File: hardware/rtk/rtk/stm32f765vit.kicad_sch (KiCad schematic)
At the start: 30 parts, among them J10 Conn_01x02_Pin, J6 MEM2052-00-195-00-A_REVA, J7 Conn_01x04_Pin, J8 Conn_01x01_Pin, J9 Conn_01x08_Pin, U3 STM32F765VITx, U5 ESP32-S3-ZERO, U6 CORE1262-868M, U7 LSM6DSOX, Y1 ASTX-H11-16.000MHZ-T

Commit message: Schematic fixes and PCB placement start: D2, C16/18/20, J4
- D2: PRTR5V0U2X → USBLC6-2SC6 (SOT-23-6), D3 removed
- C16/C18/C20: symbol → C_Polarized_Small, footprint → 0805 HandSolder
  (T529P106M010AAE200 polymer tant 10µF 10V)
- J4: footprint assigned (PinHeader 2.54mm, on/off switch)
- rtk.kicad_pcb: initial component placement begun
- Add USBLC6-2SC6 datasheet

Co-Authored-By: Claude Sonnet 4.6 <noreply@anthropic.com>
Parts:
- C16, C18, C20: footprint Capacitor_SMD:C_Elec_8x10.2 -> Capacitor_SMD:C_0805_2012Metric_Pad1.18x1.45mm_HandSolder
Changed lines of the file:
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@@
 			)
 		)
-		(property "Footprint" "Capacitor_SMD:C_Elec_8x10.2"
+		(property "Footprint" "Capacitor_SMD:C_0805_2012Metric_Pad1.18x1.45mm_HandSolder"
 			(at 269.24 133.35 0)
 			(hide yes)
@@
 			)
 		)
-		(property "Footprint" "Capacitor_SMD:C_Elec_8x10.2"
+		(property "Footprint" "Capacitor_SMD:C_0805_2012Metric_Pad1.18x1.45mm_HandSolder"
 			(at 269.24 87.63 0)
 			(hide yes)
@@
 			)
 		)
-		(property "Footprint" "Capacitor_SMD:C_Elec_8x10.2"
+		(property "Footprint" "Capacitor_SMD:C_0805_2012Metric_Pad1.18x1.45mm_HandSolder"
 			(at 269.24 36.83 0)
 			(hide yes)

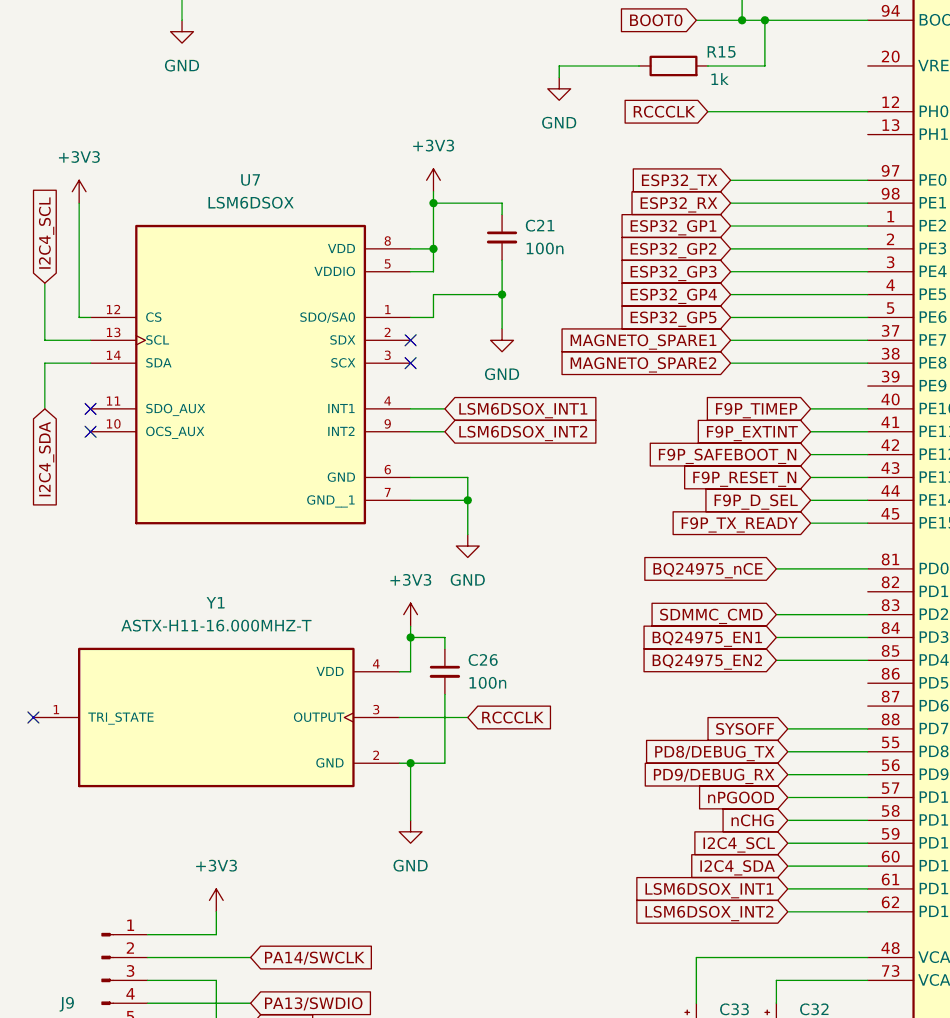
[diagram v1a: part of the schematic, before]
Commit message: PCB: round 1 initial placement complete
Most components in final positions; some will shift during routing.
Schematic tweaks picked up alongside. Add GCT USB4105 datasheet.

Co-Authored-By: Claude Sonnet 4.6 <noreply@anthropic.com>
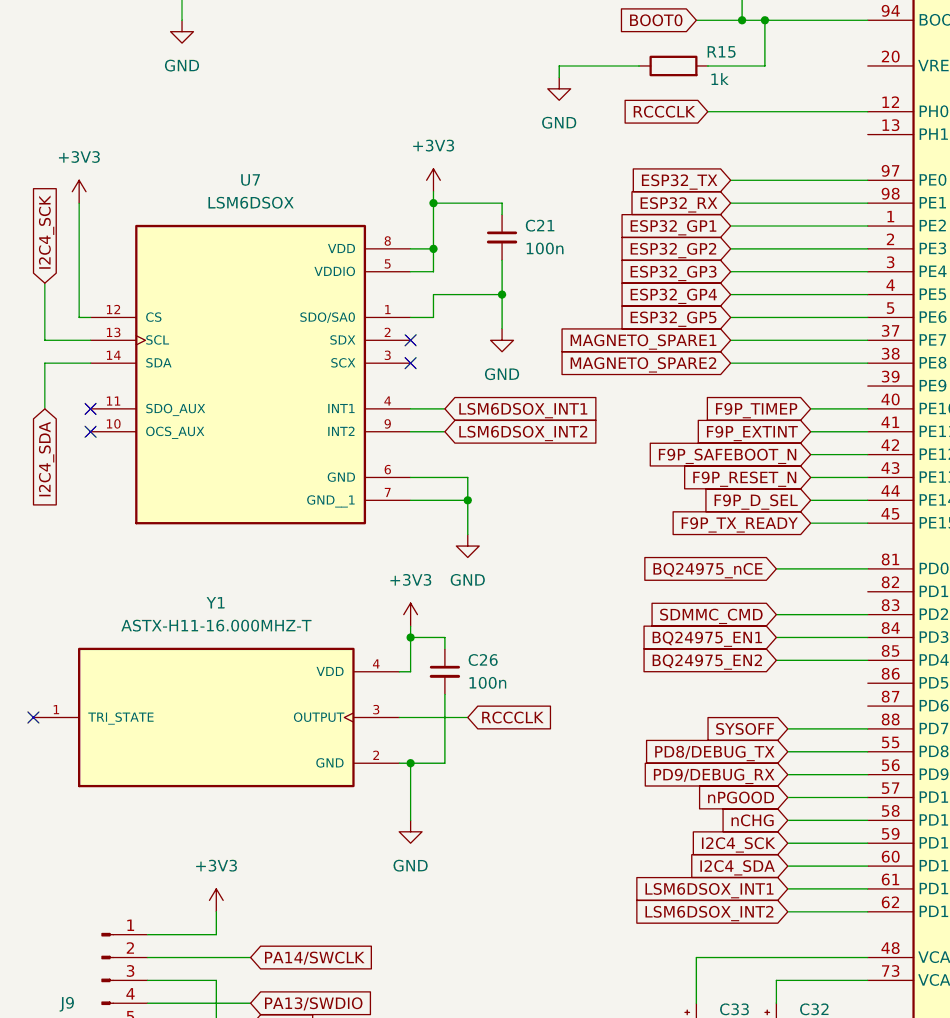
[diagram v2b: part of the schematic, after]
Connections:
- net I2C4_SCL is gone; now on net I2C4_SCK: U3.59 (PD12), U7.13 (SCL)
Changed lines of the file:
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@@
 		)
 	)
-	(global_label "I2C4_SCL"
+	(global_label "I2C4_SCK"
 		(shape input)
 		(at 99.06 137.16 180)
@@
 		)
 		(property "Intersheetrefs" "${INTERSHEET_REFS}"
-			(at 87.3058 137.16 0)
+			(at 87.0639 137.16 0)
 			(hide yes)
 			(show_name no)
@@
 		)
 	)
-	(global_label "I2C4_SCL"
+	(global_label "I2C4_SCK"
 		(shape input)
 		(at 16.51 74.93 90)
@@
 		)
 		(property "Intersheetrefs" "${INTERSHEET_REFS}"
-			(at 16.51 63.1758 90)
-			(hide yes)
-			(show_name no)
+			(at 16.51 62.9339 90)
+			(hide yes)
+			(show_name no)

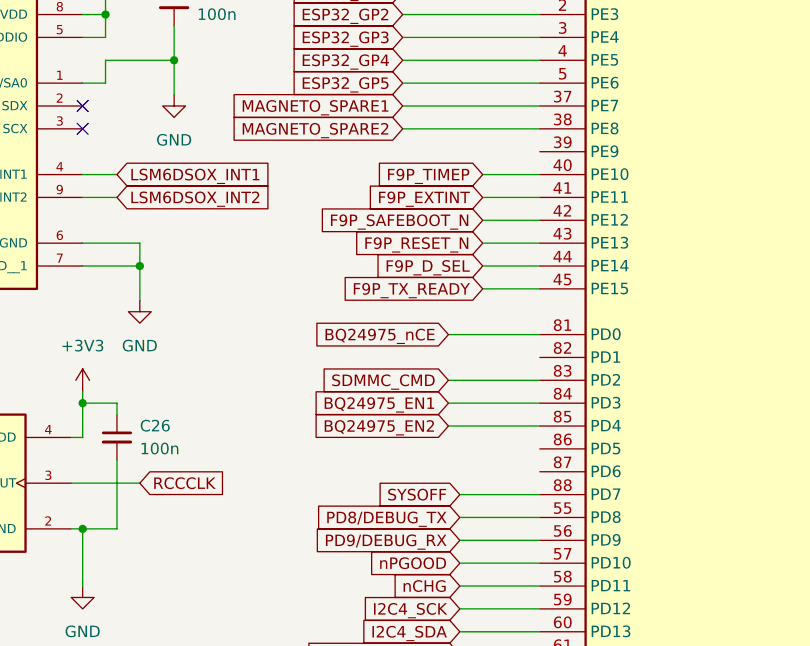
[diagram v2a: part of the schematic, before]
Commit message: Add LD3/LD4 debug LEDs: schematic, PCB placement, ioc
LD3 green PD5, LD4 red PD6 — open-drain outputs, R20/R21 1k5 pull-ups.
CubeMX regenerated with PD5/PD6 configured. Ready for routing.

Co-Authored-By: Claude Sonnet 4.6 <noreply@anthropic.com>
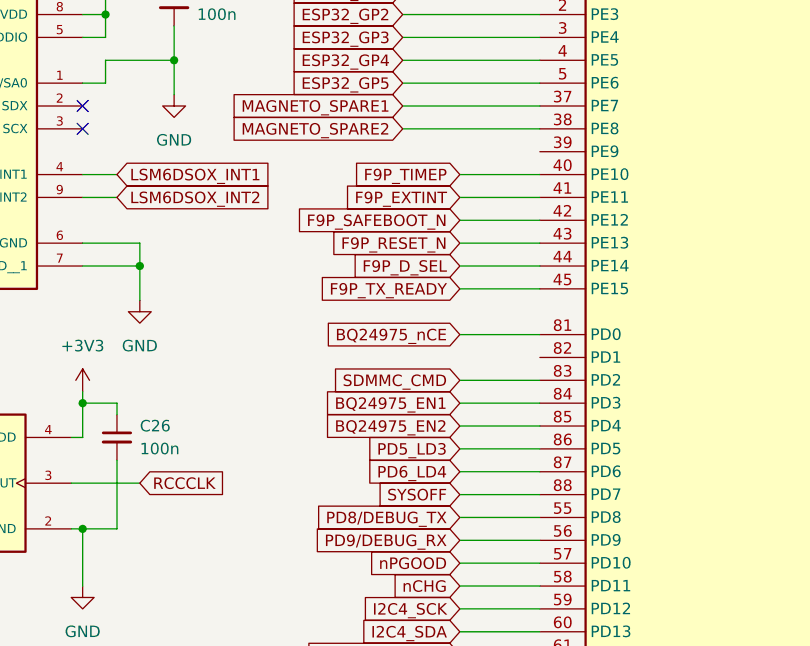
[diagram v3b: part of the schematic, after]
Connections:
- net PD5_LD3: now reaches U3.86 (PD5)
- net PD6_LD4: now reaches U3.87 (PD6)
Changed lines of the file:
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@@
 	(wire
 		(pts
-			(xy 101.6 88.9) (xy 107.95 88.9)
+			(xy 99.06 88.9) (xy 107.95 88.9)
 		)
 		(stroke
@@
 	(wire
 		(pts
-			(xy 101.6 96.52) (xy 107.95 96.52)
+			(xy 99.06 96.52) (xy 107.95 96.52)
 		)
 		(stroke
@@
 	(wire
 		(pts
-			(xy 101.6 99.06) (xy 107.95 99.06)
+			(xy 99.06 99.06) (xy 107.95 99.06)
 		)
 		(stroke
@@
 	(wire
 		(pts
+			(xy 99.06 119.38) (xy 107.95 119.38)
+		)
+		(stroke
+			(width 0)
+			(type default)
+		)
+	)
+	(wire
+		(pts
 			(xy 99.06 127) (xy 107.95 127)
 		)
@@
 	(wire
 		(pts
-			(xy 101.6 93.98) (xy 107.95 93.98)
+			(xy 99.06 93.98) (xy 107.95 93.98)
 		)
 		(stroke
@@
 	(wire
 		(pts
-			(xy 101.6 91.44) (xy 107.95 91.44)
+			(xy 99.06 91.44) (xy 107.95 91.44)
 		)
 		(stroke
@@
 	(wire
 		(pts
-			(xy 97.79 106.68) (xy 107.95 106.68)
+			(xy 99.06 106.68) (xy 107.95 106.68)
 		)
 		(stroke
@@
 	(wire
 		(pts
-			(xy 101.6 101.6) (xy 107.95 101.6)
+			(xy 99.06 101.6) (xy 107.95 101.6)
 		)
 		(stroke
@@
 	(wire
 		(pts
-			(xy 97.79 111.76) (xy 107.95 111.76)
+			(xy 99.06 111.76) (xy 107.95 111.76)
 		)
 		(stroke
@@
 	(wire
 		(pts
-			(xy 97.79 114.3) (xy 107.95 114.3)
+			(xy 99.06 114.3) (xy 107.95 114.3)
 		)
 		(stroke
@@
 	(wire
 		(pts
+			(xy 99.06 121.92) (xy 107.95 121.92)
+		)
+		(stroke
+			(width 0)
+			(type default)
+		)
+	)
+	(wire
+		(pts
 			(xy 55.88 128.27) (xy 57.15 128.27)
 		)
@@
 	(wire
 		(pts
-			(xy 97.79 116.84) (xy 107.95 116.84)
+			(xy 99.06 116.84) (xy 107.95 116.84)
 		)
 		(stroke
@@
 	(global_label "BQ24975_nCE"
 		(shape input)
-		(at 97.79 106.68 180)
+		(at 99.06 106.68 180)
 		(fields_autoplaced yes)
 		(effects
@@
 		)
 		(property "Intersheetrefs" "${INTERSHEET_REFS}"
-			(at 81.6212 106.68 0)
+			(at 82.8912 106.68 0)
 			(hide yes)
 			(show_name no)
@@
 	(global_label "F9P_SAFEBOOT_N"
 		(shape input)
-		(at 101.6 93.98 180)
+		(at 99.06 93.98 180)
 		(fields_autoplaced yes)
 		(effects
@@
 		)
 		(property "Intersheetrefs" "${INTERSHEET_REFS}"
-			(at 82.3467 93.98 0)
+			(at 79.8067 93.98 0)
 			(hide yes)
 			(show_name no)
@@
 		)
 	)
+	(global_label "PD6_LD4"
+		(shape input)
+		(at 99.06 121.92 180)
+		(fields_autoplaced yes)
+		(effects
+			(font
+				(size 1.27 1.27)
+			)
+			(justify right)
+		)
+		(property "Intersheetrefs" "${INTERSHEET_REFS}"
+			(at 87.8501 121.92 0)
+			(hide yes)
+			(show_name no)
+			(do_not_autoplace no)
+			(effects
+				(font
+					(size 1.27 1.27)
+				)
+				(justify right)
+			)
+		)
+	)
 	(global_label "SX1262_SPI2_MOSI"
 		(shape input)
@@
 	(global_label "F9P_TX_READY"
 		(shape input)
-		(at 101.6 101.6 180)
+		(at 99.06 101.6 180)
 		(fields_autoplaced yes)
 		(effects
@@
 		)
 		(property "Intersheetrefs" "${INTERSHEET_REFS}"
-			(at 85.0682 101.6 0)
+			(at 82.5282 101.6 0)
 			(hide yes)
 			(show_name no)
@@
 	(global_label "SDMMC_CMD"
 		(shape input)
-		(at 97.79 111.76 180)
+		(at 99.06 111.76 180)
 		(fields_autoplaced yes)
 		(effects
@@
 		)
 		(property "Intersheetrefs" "${INTERSHEET_REFS}"
-			(at 83.1935 111.76 0)
+			(at 84.4635 111.76 0)
 			(hide yes)
 			(show_name no)
@@
 	(global_label "F9P_RESET_N"
 		(shape input)
-		(at 101.6 96.52 180)
+		(at 99.06 96.52 180)
 		(fields_autoplaced yes)
 		(effects
@@
 		)
 		(property "Intersheetrefs" "${INTERSHEET_REFS}"
-			(at 86.0359 96.52 0)
+			(at 83.4959 96.52 0)
 			(hide yes)
 			(show_name no)
@@
 	(global_label "F9P_D_SEL"
 		(shape input)
-		(at 101.6 99.06 180)
+		(at 99.06 99.06 180)
 		(fields_autoplaced yes)
 		(effects
@@
 		)
 		(property "Intersheetrefs" "${INTERSHEET_REFS}"
-			(at 88.4549 99.06 0)
+			(at 85.9149 99.06 0)
 			(hide yes)
 			(show_name no)
@@
 		)
 	)
+	(global_label "PD5_LD3"
+		(shape input)
+		(at 99.06 119.38 180)
+		(fields_autoplaced yes)
+		(effects
+			(font
+				(size 1.27 1.27)
+			)
+			(justify right)
+		)
+		(property "Intersheetrefs" "${INTERSHEET_REFS}"
+			(at 87.8501 119.38 0)
+			(hide yes)
+			(show_name no)
+			(do_not_autoplace no)
+			(effects
+				(font
+					(size 1.27 1.27)
+				)
+				(justify right)
+			)
+		)
+	)
 	(global_label "F9P_ANT_SHORT"
 		(shape input)
@@
 	(global_label "F9P_EXTINT"
 		(shape input)
-		(at 101.6 91.44 180)
+		(at 99.06 91.44 180)
 		(fields_autoplaced yes)
 		(effects
@@
 		)
 		(property "Intersheetrefs" "${INTERSHEET_REFS}"
-			(at 87.8501 91.44 0)
+			(at 85.3101 91.44 0)
 			(hide yes)
 			(show_name no)
@@
 	(global_label "BQ24975_EN1"
 		(shape input)
-		(at 97.79 114.3 180)
+		(at 99.06 114.3 180)
 		(fields_autoplaced yes)
 		(effects
@@
 		)
 		(property "Intersheetrefs" "${INTERSHEET_REFS}"
-			(at 81.5002 114.3 0)
+			(at 82.7702 114.3 0)
 			(hide yes)
 			(show_name no)
@@
 	(global_label "BQ24975_EN2"
 		(shape input)
-		(at 97.79 116.84 180)
+		(at 99.06 116.84 180)
 		(fields_autoplaced yes)
 		(effects
@@
 		)
 		(property "Intersheetrefs" "${INTERSHEET_REFS}"
-			(at 81.5002 116.84 0)
+			(at 82.7702 116.84 0)
 			(hide yes)
 			(show_name no)
@@
 	(global_label "F9P_TIMEP"
 		(shape input)
-		(at 101.6 88.9 180)
+		(at 99.06 88.9 180)
 		(fields_autoplaced yes)
 		(effects
@@
 		)
 		(property "Intersheetrefs" "${INTERSHEET_REFS}"
-			(at 88.6363 88.9 0)
+			(at 86.0963 88.9 0)
 			(hide yes)
 			(show_name no)

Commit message: Add VBAT monitor: 100k divider to PA1 ADC1_IN1
Two 100k resistors divide VBAT by 2 (VBAT_2) fed to PA1. CubeMX
regenerated with ADC1 IN1 on PA1. HAL ADC driver files added.

Co-Authored-By: Claude Sonnet 4.6 <noreply@anthropic.com>
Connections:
- net VBAT_2: now reaches U3.23 (PA1)
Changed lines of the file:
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@@
 	(wire
 		(pts
+			(xy 153.67 43.18) (xy 163.83 43.18)
+		)
+		(stroke
+			(width 0)
+			(type default)
+		)
+	)
+	(wire
+		(pts
 			(xy 41.91 177.8) (xy 52.07 177.8)
 		)
@@
 			)
 		)
+	)
+	(global_label "VBAT_2"
+		(shape input)
+		(at 163.83 43.18 0)
+		(fields_autoplaced yes)
+		(effects
+			(font
+				(size 1.27 1.27)
+			)
+			(justify left)
+		)
+		(property "Intersheetrefs" "${INTERSHEET_REFS}"
+			(at 173.4071 43.18 0)
+			(hide yes)
+			(show_name no)
+			(do_not_autoplace no)
+			(effects
+				(font
+					(size 1.27 1.27)
+				)
+				(justify left)
+			)
+		)

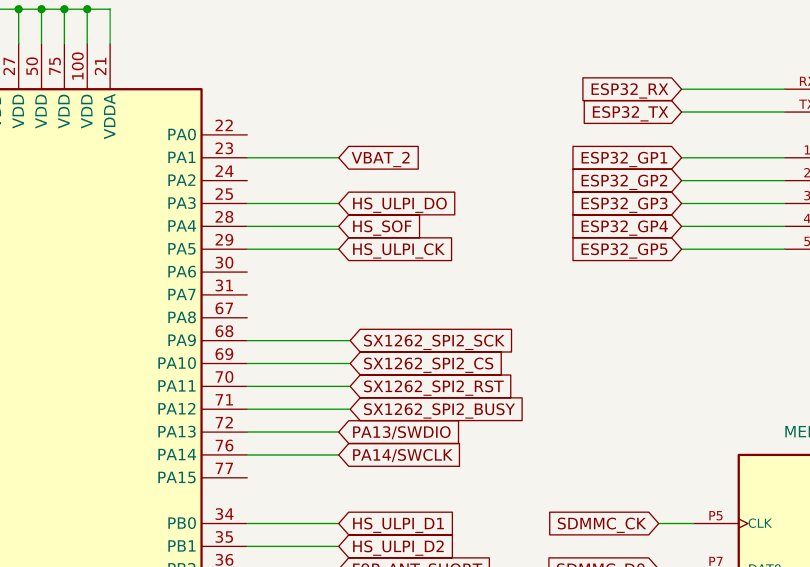
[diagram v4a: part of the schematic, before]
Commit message: PCB: initial routing complete, pre-DRC snapshot
All signals routed including USB3300 VDD1.8 (pins 15/26 opposite sides,
long perimeter route). Ready for design rules checks.

Co-Authored-By: Claude Sonnet 4.6 <noreply@anthropic.com>
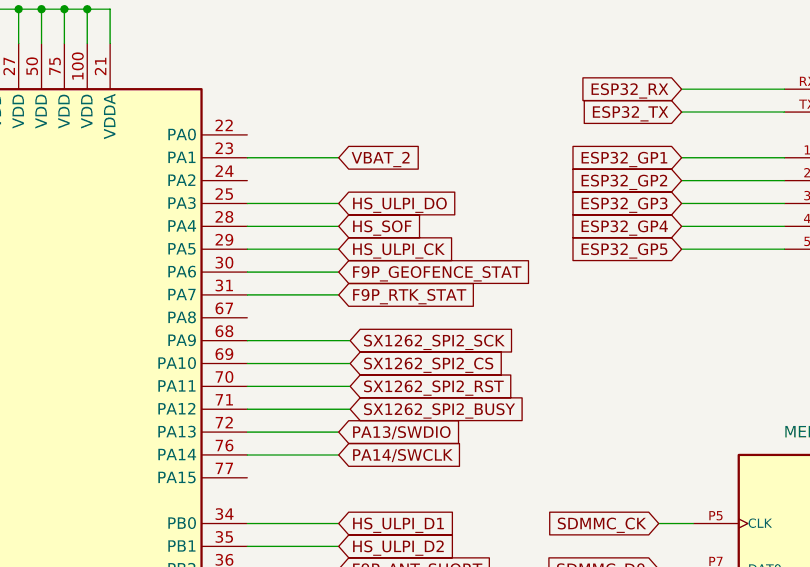
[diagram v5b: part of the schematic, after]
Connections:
- net F9P_GEOFENCE_STAT: now reaches U3.30 (PA6)
- net F9P_RTK_STAT: now reaches U3.31 (PA7)
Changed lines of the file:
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@@
+	(wire
+		(pts
+			(xy 153.67 55.88) (xy 163.83 55.88)
+		)
+		(stroke
+			(width 0)
+			(type default)
+		)
+	)
 	(wire
 		(pts
@@
 	(wire
 		(pts
+			(xy 153.67 58.42) (xy 163.83 58.42)
+		)
+		(stroke
+			(width 0)
+			(type default)
+		)
+	)
+	(wire
+		(pts
 			(xy 269.24 130.81) (xy 269.24 125.73)
 		)
@@
 		)
 	)
+	(global_label "F9P_RTK_STAT"
+		(shape input)
+		(at 163.83 58.42 0)
+		(fields_autoplaced yes)
+		(effects
+			(font
+				(size 1.27 1.27)
+			)
+			(justify left)
+		)
+		(property "Intersheetrefs" "${INTERSHEET_REFS}"
+			(at 180.0594 58.42 0)
+			(hide yes)
+			(show_name no)
+			(do_not_autoplace no)
+			(effects
+				(font
+					(size 1.27 1.27)
+				)
+				(justify left)
+			)
+		)
+	)
 	(global_label "I2C4_SDA"
 		(shape input)
@@
 			)
 		)
+	)
+	(global_label "F9P_GEOFENCE_STAT"
+		(shape input)
+		(at 163.83 55.88 0)
+		(fields_autoplaced yes)
+		(effects
+			(font
+				(size 1.27 1.27)
+			)
+			(justify left)
+		)
+		(property "Intersheetrefs" "${INTERSHEET_REFS}"
+			(at 186.2884 55.88 0)
+			(hide yes)
+			(show_name no)
+			(do_not_autoplace no)
+			(effects
+				(font
+					(size 1.27 1.27)
+				)
+				(justify left)
+			)
+		)
